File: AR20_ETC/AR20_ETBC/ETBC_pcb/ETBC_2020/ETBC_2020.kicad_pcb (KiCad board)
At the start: 2 copper layers, 31 parts, among them IC1 MC33931EK, J1 Conn_02x09_Top_Bottom, Q1 NDS356AP, U1 ACM_2020

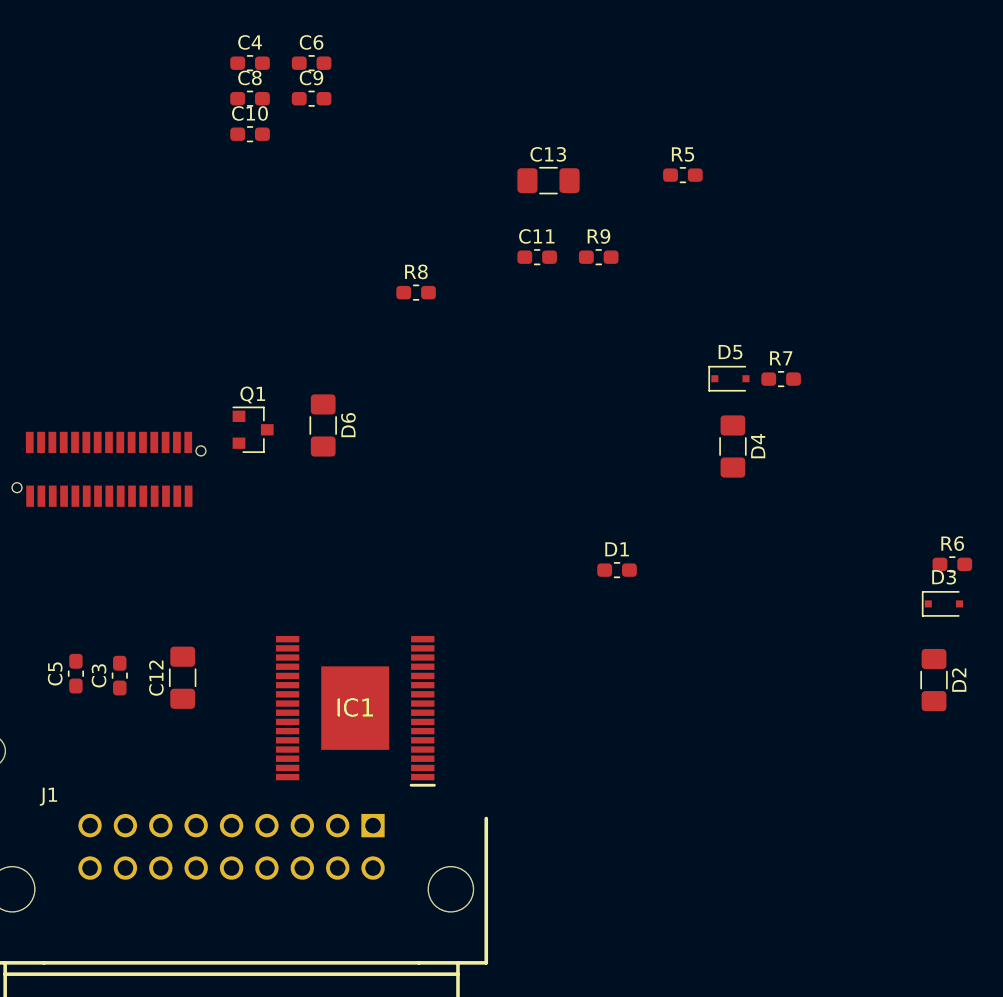
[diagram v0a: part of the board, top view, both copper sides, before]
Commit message: Adjusted footprints and created BOM
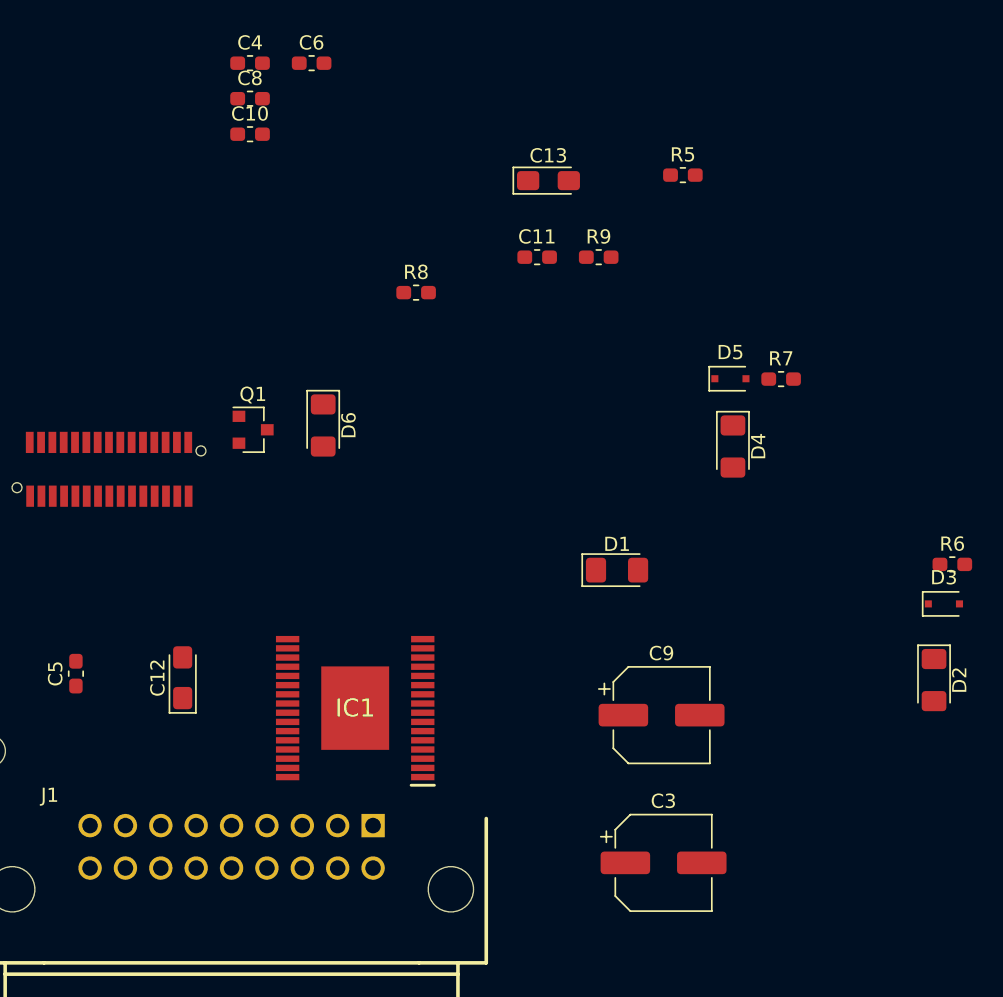
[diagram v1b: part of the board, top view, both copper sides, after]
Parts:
- C1, C2: value C_Small -> 0.1uF
- C10: value 33nF -> 0.033uF
- C11, C5: value 100nF -> 0.1uF
- C12, C13: footprint Capacitor_SMD:C_1206_3216Metric_Pad1.42x1.75mm_HandSolder -> Capacitor_Tantalum_SMD:CP_EIA-3216-10_Kemet-I_Pad1.58x1.35mm_HandSolder
- C3, C9: value 250uF -> 220uF; footprint Capacitor_SMD:C_0603_1608Metric_Pad1.05x0.95mm_HandSolder -> Capacitor_SMD:CP_Elec_6.3x7.7
- C6, C8: value 10nF -> 0.01uF
- D1: footprint Capacitor_SMD:C_0603_1608Metric_Pad1.05x0.95mm_HandSolder -> Diode_SMD:D_1206_3216Metric_Pad1.42x1.75mm_HandSolder
- D2, D4, D6: footprint Capacitor_SMD:C_1206_3216Metric_Pad1.42x1.75mm_HandSolder -> Diode_SMD:D_1206_3216Metric_Pad1.42x1.75mm_HandSolder
- R1, R2: value R_Small -> 8K2
- moved C9 50.1 mm to (130.4, 87.7)
- moved C3 40.6 mm to (130.5, 98.1), turned to 0 degrees

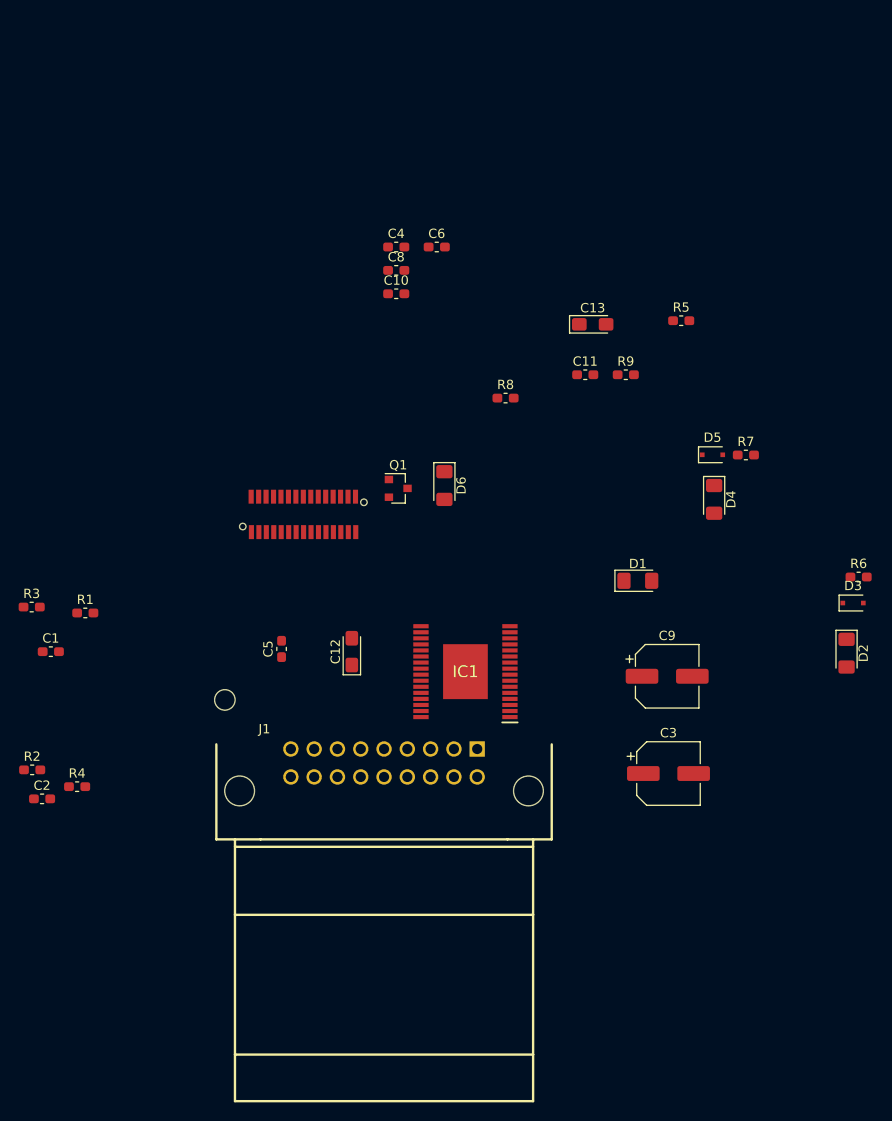
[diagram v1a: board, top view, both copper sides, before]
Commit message: ETBC Semi complete - Evryting connected. Check description
Neec to check all footprints.
Need to check all symbols (Pin numbering correspond to footprint and datasheet)
Need to check JLCPCB DRC settings.
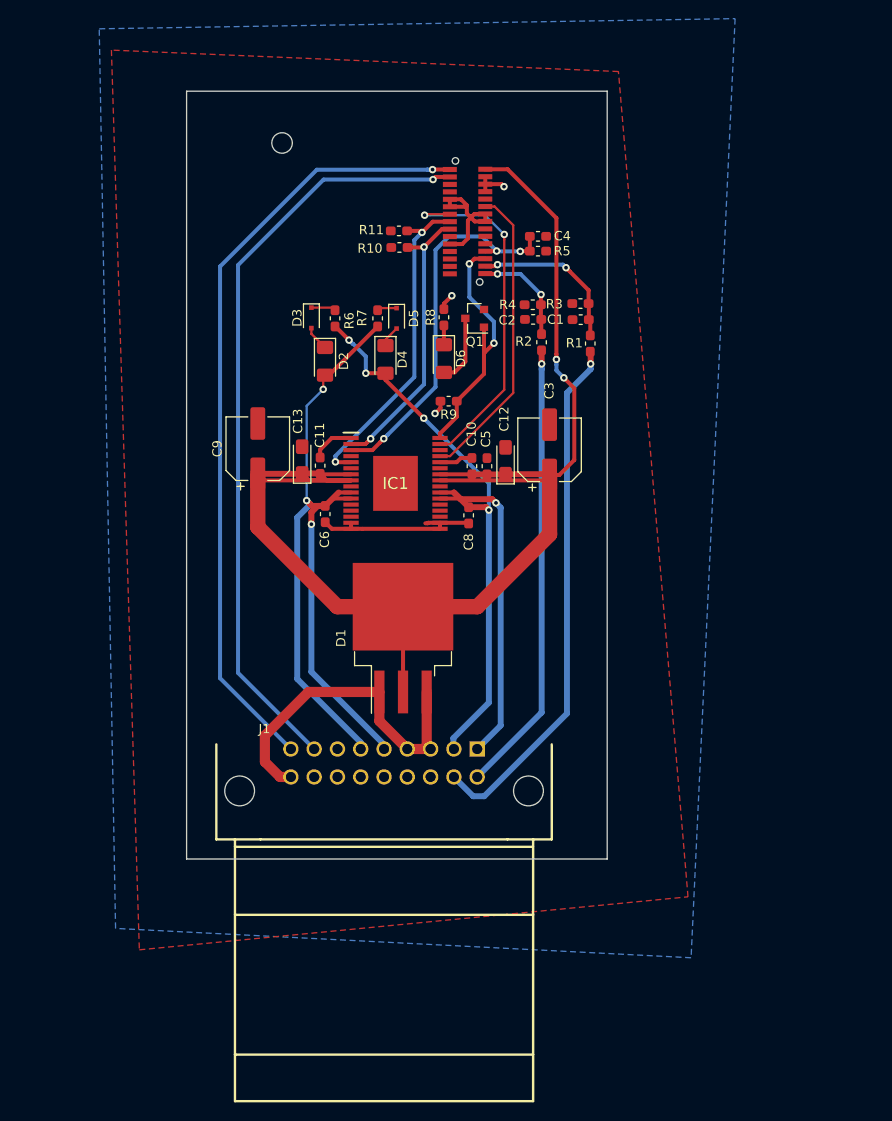
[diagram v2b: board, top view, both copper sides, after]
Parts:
- added R10: 4.7K, Resistor_SMD:R_0603_1608Metric_Pad1.05x0.95mm_HandSolder, F.Cu at (101.7, 41.7)
- added R11: 4.7K, Resistor_SMD:R_0603_1608Metric_Pad1.05x0.95mm_HandSolder, F.Cu at (101.6, 39.9)
- C4: value 0.047uF -> 1uF
- D1: value DCBU0340-HF -> WNS20S100CB; footprint Diode_SMD:D_1206_3216Metric_Pad1.42x1.75mm_HandSolder -> Package_TO_SOT_SMD:TO-263-3_TabPin2
- R5: value 270 -> 255
- moved C2 73.7 mm to (116.0, 49.4), turned to 180 degrees
- moved R2 71.4 mm to (116.9, 51.8), turned to 270 degrees
- moved R4 71.2 mm to (116.0, 47.8), turned to 180 degrees
- moved R3 67.3 mm to (121.1, 47.7), turned to 180 degrees
- moved C1 67.1 mm to (121.1, 49.4), turned to 180 degrees
- moved D3 65.7 mm to (92.2, 49.2), turned to 270 degrees
- moved D2 64.2 mm to (93.7, 53.9)
- moved R6 62.7 mm to (94.7, 49.3), turned to 270 degrees
- moved R1 61.4 mm to (122.1, 52.0), turned to 270 degrees
- moved C9 50.3 mm to (86.4, 63.3), turned to 90 degrees
- moved R7 42.2 mm to (99.3, 49.3), turned to 270 degrees
- moved D4 38.3 mm to (100.2, 53.7)
- moved C3 37.0 mm to (117.8, 63.4), turned to 90 degrees
- moved D5 36.9 mm to (101.3, 49.3), turned to 270 degrees
- moved U1 36.0 mm to (109.0, 38.9), turned to 270 degrees
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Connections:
- D1 pad 1: GND -> 12V
- J1 pad 1: OUT1 -> OUT2
- J1 pad 10: GND -> TPS2
- J1 pad 11: GND -> TPS1
- J1 pad 12: Net-(J1-Pad12) -> GND
- J1 pad 13: Net-(J1-Pad13) -> GND
- J1 pad 15: Net-(J1-Pad15) -> +5V
- J1 pad 16: Net-(J1-Pad16) -> +5V
- J1 pad 17: CANH -> GND
- J1 pad 18: CANL -> 12V
- J1 pad 2: OUT1 -> OUT2
- J1 pad 3: PWR -> 12V
- J1 pad 4: PWR -> 12V
- J1 pad 5: OUT2 -> OUT1
- J1 pad 6: OUT2 -> OUT1
- J1 pad 8: Net-(J1-Pad8) -> CANH
- J1 pad 9: Net-(J1-Pad9) -> CANL
- U1 pad 17: Net-(U1-Pad17) -> PWM_10
- U1 pad 20: Net-(U1-Pad20) -> PWM_3
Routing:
- net PWR: track 0.00 -> 152.5 mm, vias 0 -> 2
- net OUT2: track 0.00 -> 97.2 mm, vias 0 -> 5
- net OUT1: track 0.00 -> 91.7 mm, vias 0 -> 3
- net CANL: track 0.00 -> 83.9 mm, vias 0 -> 1
- net CANH: track 0.00 -> 82.0 mm, vias 0 -> 1
- net TPS1: track 0.00 -> 56.6 mm, vias 0 -> 1
- net TPS2: track 0.00 -> 48.8 mm, vias 0 -> 1
- net Feedback: track 0.00 -> 40.8 mm, vias 0 -> 3
- net GND: track 0.00 -> 38.3 mm
- net PWM_10: track 0.00 -> 38.1 mm, vias 0 -> 2
- net 12V: track 0.00 -> 36.7 mm
- net EN_D2: track 0.00 -> 35.3 mm, vias 0 -> 2
- net PWM_3: track 0.00 -> 32.5 mm
- net D1: track 0.00 -> 30.7 mm, vias 0 -> 2
- net SFlag: track 0.00 -> 26.9 mm, vias 0 -> 2
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- added copper zone on B.Cu, net +5V
- added copper zone on F.Cu, net GND
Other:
- board outline added: 45.1 x 82.4 mm

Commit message: ETBC Complete
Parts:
- added H1: MountingHole_Pad, MountingHole:MountingHole_3.2mm_M3_Pad_Via, F.Cu at (88.0, 82.0)
- added H2: MountingHole_Pad, MountingHole:MountingHole_3.2mm_M3_Pad_Via, F.Cu at (119.0, 30.0)
- added TP1: PWM3, TestPoint:TestPoint_Keystone_5000-5004_Miniature, F.Cu at (80.0, 28.0)
- added TP10: PWM10_Motor, TestPoint:TestPoint_Keystone_5000-5004_Miniature, F.Cu at (120.7, 80.0)
- added TP2: PWM10, TestPoint:TestPoint_Keystone_5000-5004_Miniature, F.Cu at (80.0, 33.1)
- added TP3: D2, TestPoint:TestPoint_Keystone_5000-5004_Miniature, F.Cu at (80.0, 38.2)
- added TP4: D1, TestPoint:TestPoint_Keystone_5000-5004_Miniature, F.Cu at (80.0, 43.2)
- added TP5: Feed, TestPoint:TestPoint_Keystone_5000-5004_Miniature, F.Cu at (80.0, 53.4)
- added TP6: Flag, TestPoint:TestPoint_Keystone_5000-5004_Miniature, F.Cu at (80.0, 48.3)
- added TP7: TPS1F, TestPoint:TestPoint_Keystone_5000-5004_Miniature, F.Cu at (120.7, 42.9)
- added TP8: TPS2F, TestPoint:TestPoint_Keystone_5000-5004_Miniature, F.Cu at (120.6, 37.8)
- added TP9: PWM3_Motor, TestPoint:TestPoint_Keystone_5000-5004_Miniature, F.Cu at (120.7, 85.1)
- moved C6 0.65 mm to (94.0, 70.9)
- moved C8 0.63 mm to (108.6, 70.9)
- moved Q1 0.28 mm to (109.7, 49.6)
- moved R8 0.13 mm to (106.5, 49.3), turned to 270 degrees
- turned D6 to 90 degrees
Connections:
- D6 pad 1: Net-(D6-Pad1) -> GND
- Q1 pad 2: GND -> +5V
- Q1 pad 3: Net-(D6-Pad2) -> Net-(Q1-Pad3)
- R8 pad 1: Net-(D6-Pad1) -> Net-(Q1-Pad3)
- R8 pad 2: +5V -> Net-(D6-Pad2)
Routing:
- net PWM_3: track 32.5 -> 74.5 mm, vias 0 -> 2
- net OUT2: track 97.2 -> 56.7 mm, vias 5 -> 8
- net Feedback: track 40.8 -> 74.5 mm, vias 3 -> 4
- net SFlag: track 26.9 -> 54.9 mm, vias 2 -> 0
- net PWM_10: track 38.1 -> 65.9 mm
- net D1: track 30.7 -> 56.2 mm
- net EN_D2: track 35.3 -> 58.9 mm
- net OUT1: track 91.7 -> 70.3 mm, vias 3 -> 7
- net TPS2_Filtered: track 11.2 -> 22.6 mm, vias 2 -> 3
- net CANL: track 83.9 -> 77.2 mm
- net CANH: track 82.0 -> 75.7 mm
- net Net-(D6-Pad2): track 7.43 -> 1.98 mm
- net GND: track 38.3 -> 33.3 mm, vias 0 -> 1
- net Net-(Q1-Pad3): track 0.00 -> 2.74 mm
- net TPS1_Filtered: track 17.2 -> 19.6 mm
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- added copper zone on B.Cu, net OUT1
- added copper zone on B.Cu, net OUT2
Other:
- board size 45.1 x 82.4 mm -> 48 x 82.4 mm
- rule via_min_size: 0.4 -> 0.3
- board text added: "Bachelor Thesis 2020 Electronic Throttle Body Controller V1.0"
- board text added: "FAULT"
- board text added: "FWD"
- board text added: "REV"
